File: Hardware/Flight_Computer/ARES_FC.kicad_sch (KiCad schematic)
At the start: 46 parts, among them J1 SWD, J2 TYPE-C-31-M-12, J4 5V, J5 GND, U1 STM32F401CCU6, U2 AMS1117-3.3, U3 BMP280, U4 BNO055, U5 W25Q32JVSS, Y1 16MHz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

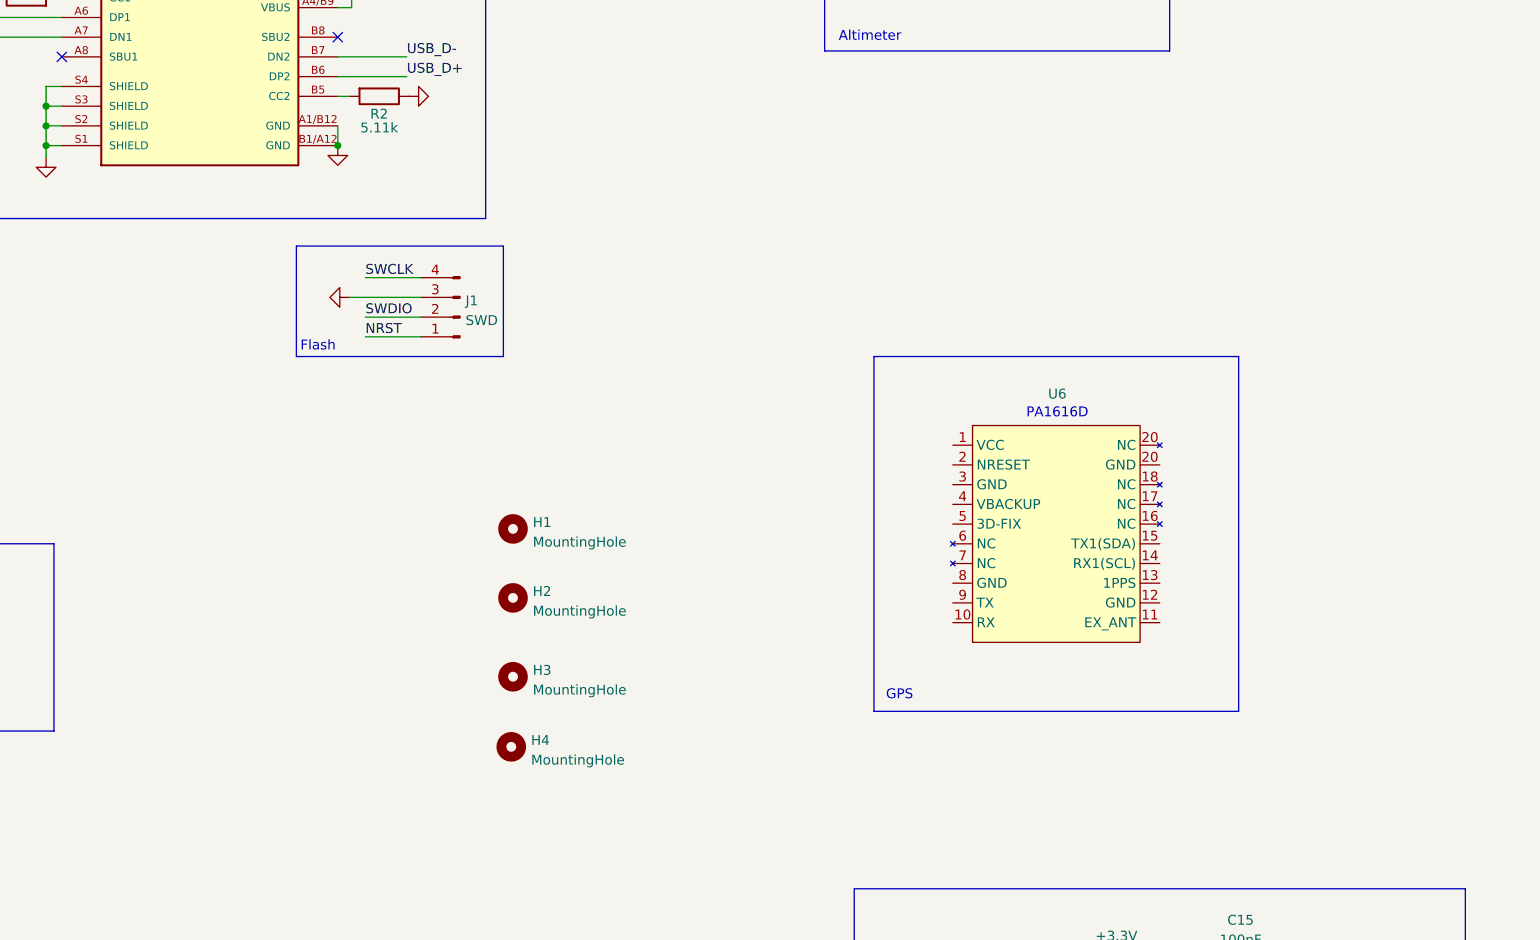
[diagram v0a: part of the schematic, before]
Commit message: started filling out GPS schematic
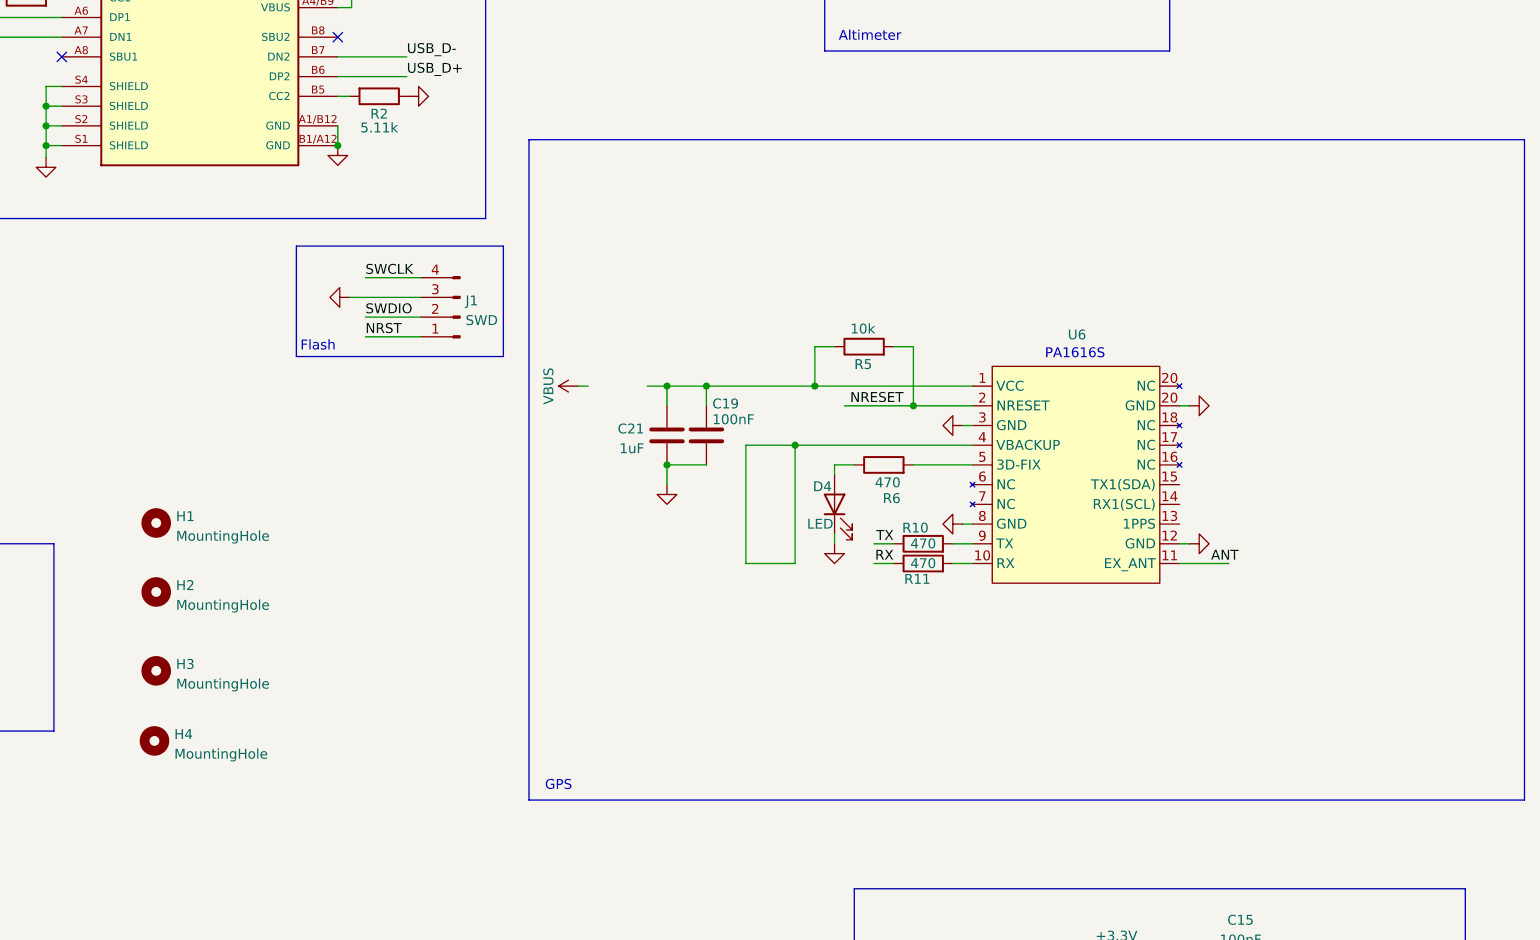
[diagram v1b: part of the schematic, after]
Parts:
- added C19: 100nF, Capacitor_SMD:C_0402_1005Metric, symbol Device:C
- added C21: 1uF, Capacitor_SMD:C_0402_1005Metric, symbol Device:C
- added D4: LED, LED_SMD:LED_0603_1608Metric, symbol Device:LED
- added R10, R11, R6: 470, Resistor_SMD:R_0402_1005Metric, symbol Device:R
- added R5: 10k, Resistor_SMD:R_0402_1005Metric, symbol Device:R
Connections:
- net GND: now also U6.12 (GND), U6.20 (NC), U6.3 (GND), U6.8 (GND), C19.2, C21.2, D4.1 (K)
- net at U6.1 (VCC): now also C19.1, C21.1, R5.1
- net at U6.10 (RX): now also R11.2
- net NRESET: now reaches U6.2 (NRESET)
- net NRESET: now also R5.2
- net at U6.5 (3D-FIX): now also R6.2
- net at U6.9 (TX): now also R10.2
- new net: D4.2 (A), R6.1
- new net RX: R11.1
- new net TX: R10.1
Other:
- note added: "PA1616S"
- note removed: "PA1616D"
- moved on the sheet: H1, H2, H3, H4, U6

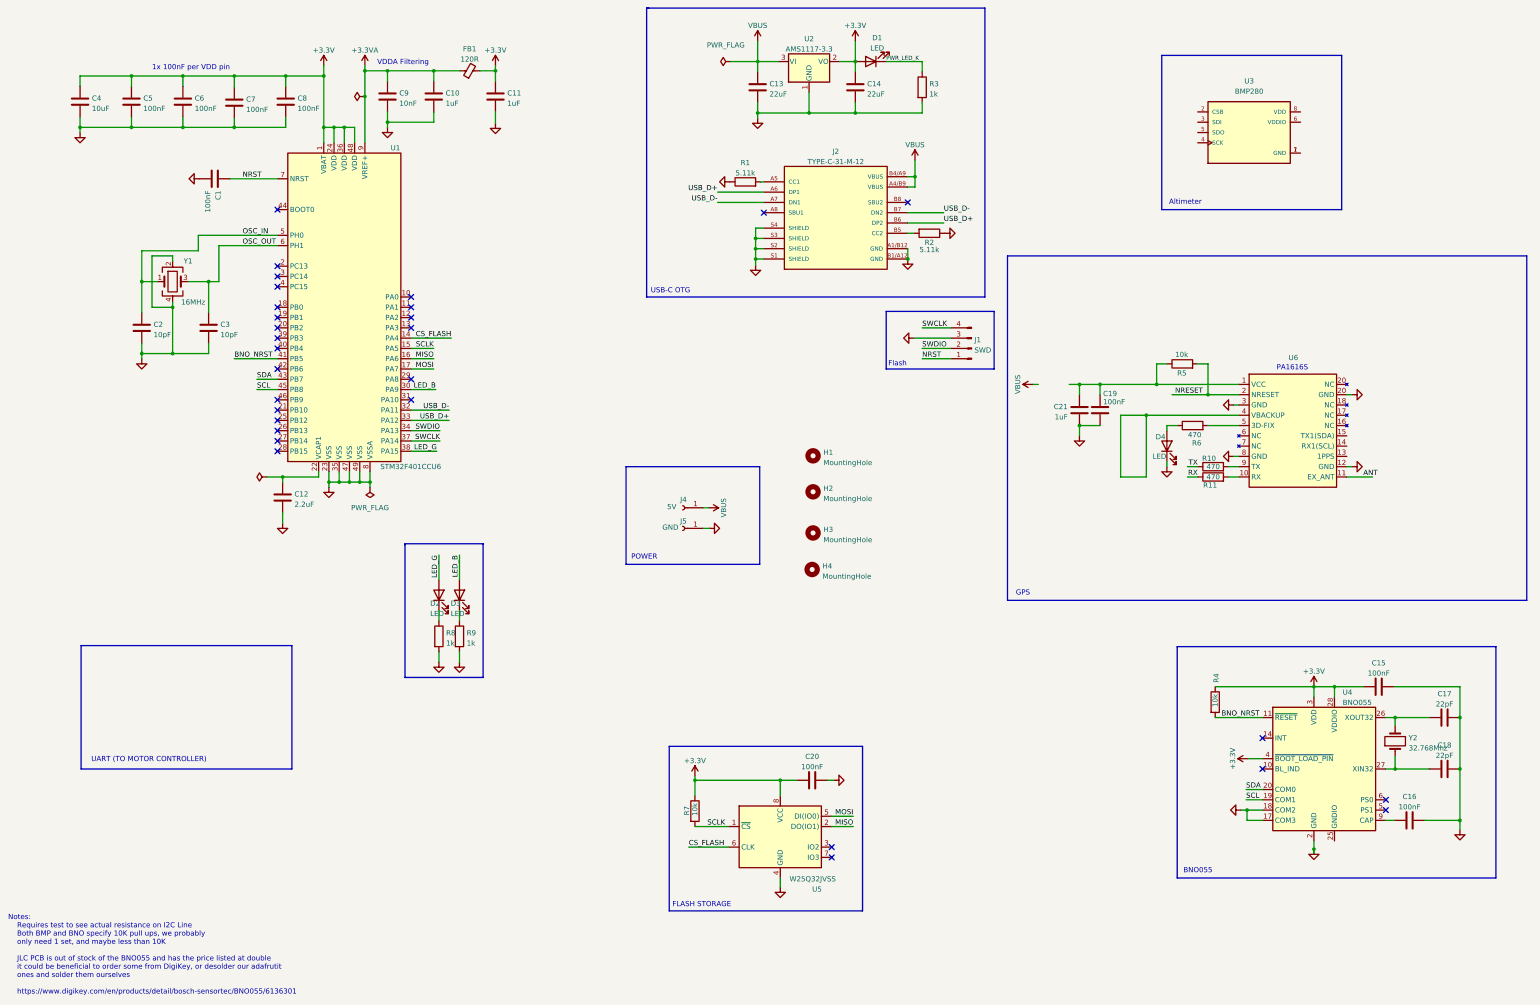
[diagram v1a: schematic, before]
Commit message: finished GPS schematic
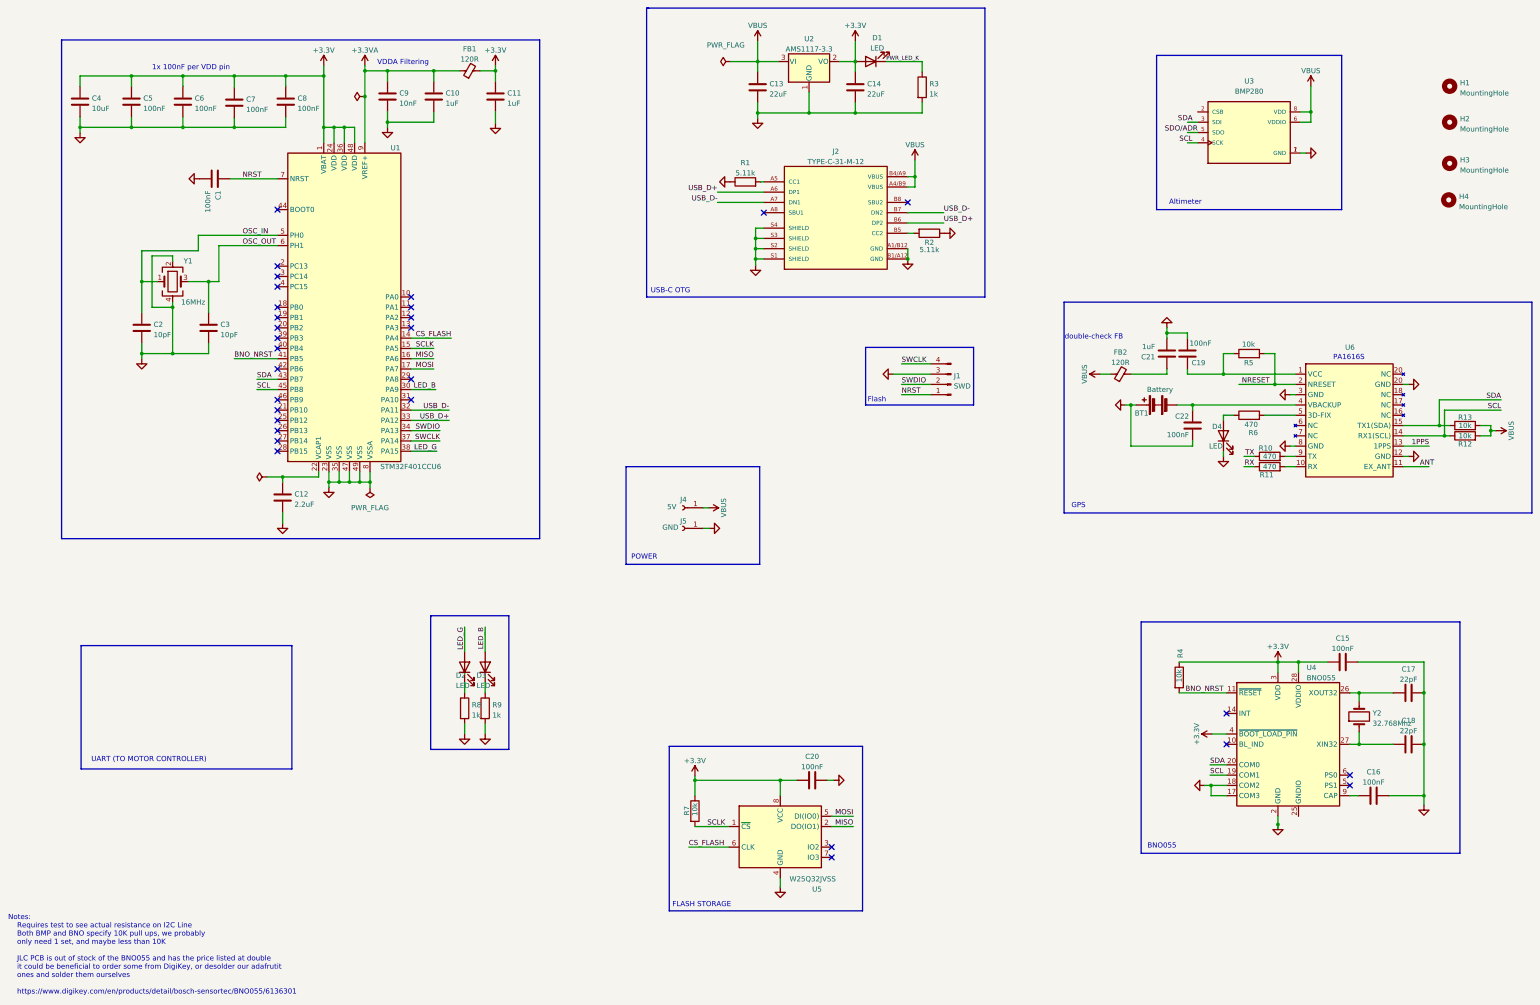
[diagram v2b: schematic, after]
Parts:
- added BT1: Battery, symbol Device:Battery
- added C22: 100nF, Capacitor_SMD:C_0402_1005Metric, symbol Device:C
- added FB2: 120R, Inductor_SMD:L_0603_1608Metric, symbol Device:FerriteBead_Small
- added R12, R13: 10k, symbol Device:R
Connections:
- net GND: now also U3.1 (GND), U3.7 (GND), BT1.1 (+), C22.2
- net SCL: now also U3.4 (SCK), U6.14 (RX1(SCL)), R12.1
- net SDA: now also U3.3 (SDI), U6.15 (TX1(SDA)), R13.1
- net VBUS: now also U3.6 (VDDIO), U3.8 (VDD), FB2.1, R12.2, R13.2
- net at C19.1, R5.1, U6.1 (VCC): no longer C21.1
- net 1PPS: now reaches U6.13 (1PPS)
- net at U6.4 (VBACKUP): now also BT1.2 (-), C22.1
- net SDO/ADR: now reaches U3.5 (SDO)
- new net: C21.1, FB2.2
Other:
- note added: "double-check FB"
- moved on the sheet: C15, C16, C17, C18, C19, C21, D2, D3, D4, H1, H2, H3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

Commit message: finished schematic for MBP280, GPS and UARTs
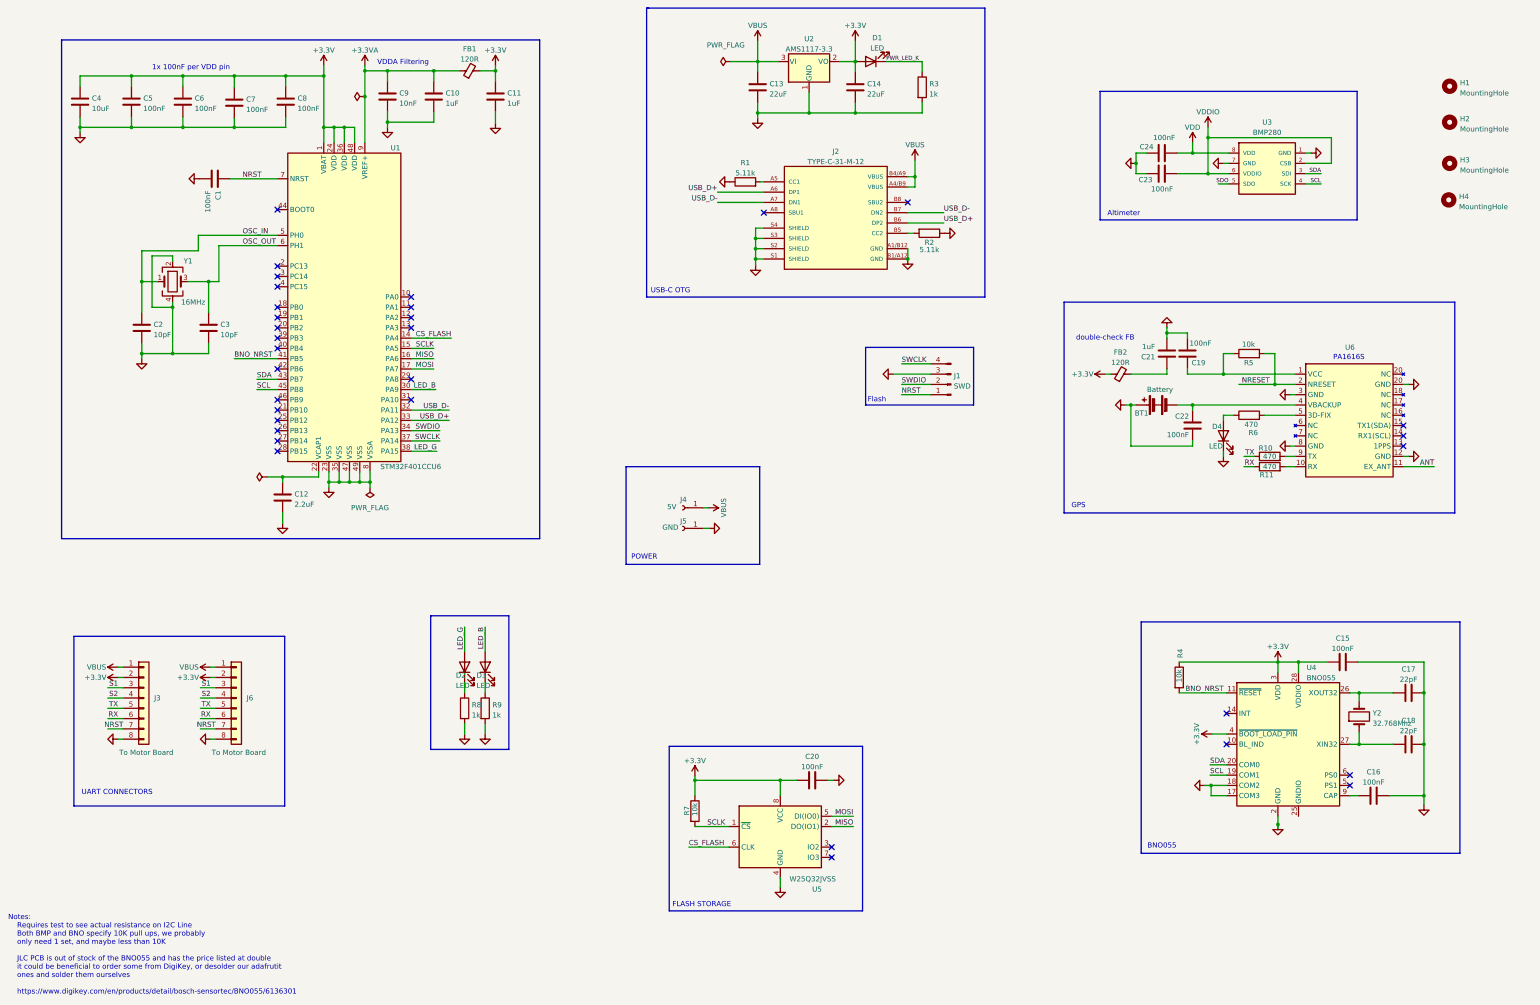
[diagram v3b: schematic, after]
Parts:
- removed R12, R13: 10k, symbol Device:R
- added C23, C24: 100nF, Capacitor_SMD:C_0402_1005Metric, symbol Device:C
- added J3, J6: To Motor Board, symbol Connector_Generic:Conn_01x08
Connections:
- net +3.3V: now also FB2.1, J3.2 (Pin_2), J6.2 (Pin_2)
- net ANT: now also U6.11 (EX_ANT)
- net GND: now also C23.1, C24.1, J3.8 (Pin_8), J6.8 (Pin_8)
- net NRST: now also J3.7 (Pin_7), J6.7 (Pin_7)
- net RX: now also J3.6 (Pin_6), J6.6 (Pin_6)
- net SCL: no longer U6.14 (RX1(SCL))
- net SDA: no longer U6.15 (TX1(SDA))
- net TX: now also J3.5 (Pin_5), J6.5 (Pin_5)
- net VBUS: now also J3.1 (Pin_1), J6.1 (Pin_1); no longer FB2.1, U3.6 (VDDIO), U3.8 (VDD)
- net VDDIO: now reaches U3.2 (CSB)
- net VDDIO: now also U3.6 (VDDIO), C23.2
- net 1PPS: no longer names the net of U6.13 (1PPS)
- net SDO/ADR renamed SDO
- new net S1: J3.3 (Pin_3), J6.3 (Pin_3)
- new net S2: J3.4 (Pin_4), J6.4 (Pin_4)
- new net VDD: C24.2, U3.8 (VDD)
- no-connect marks 30 -> 33
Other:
- note added: "UART CONNECTORS"
- note removed: "UART (TO MOTOR CONTROLLER)"

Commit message: Fixed "RCS Board Problems"
in RCS Board Problems Discord Thread.
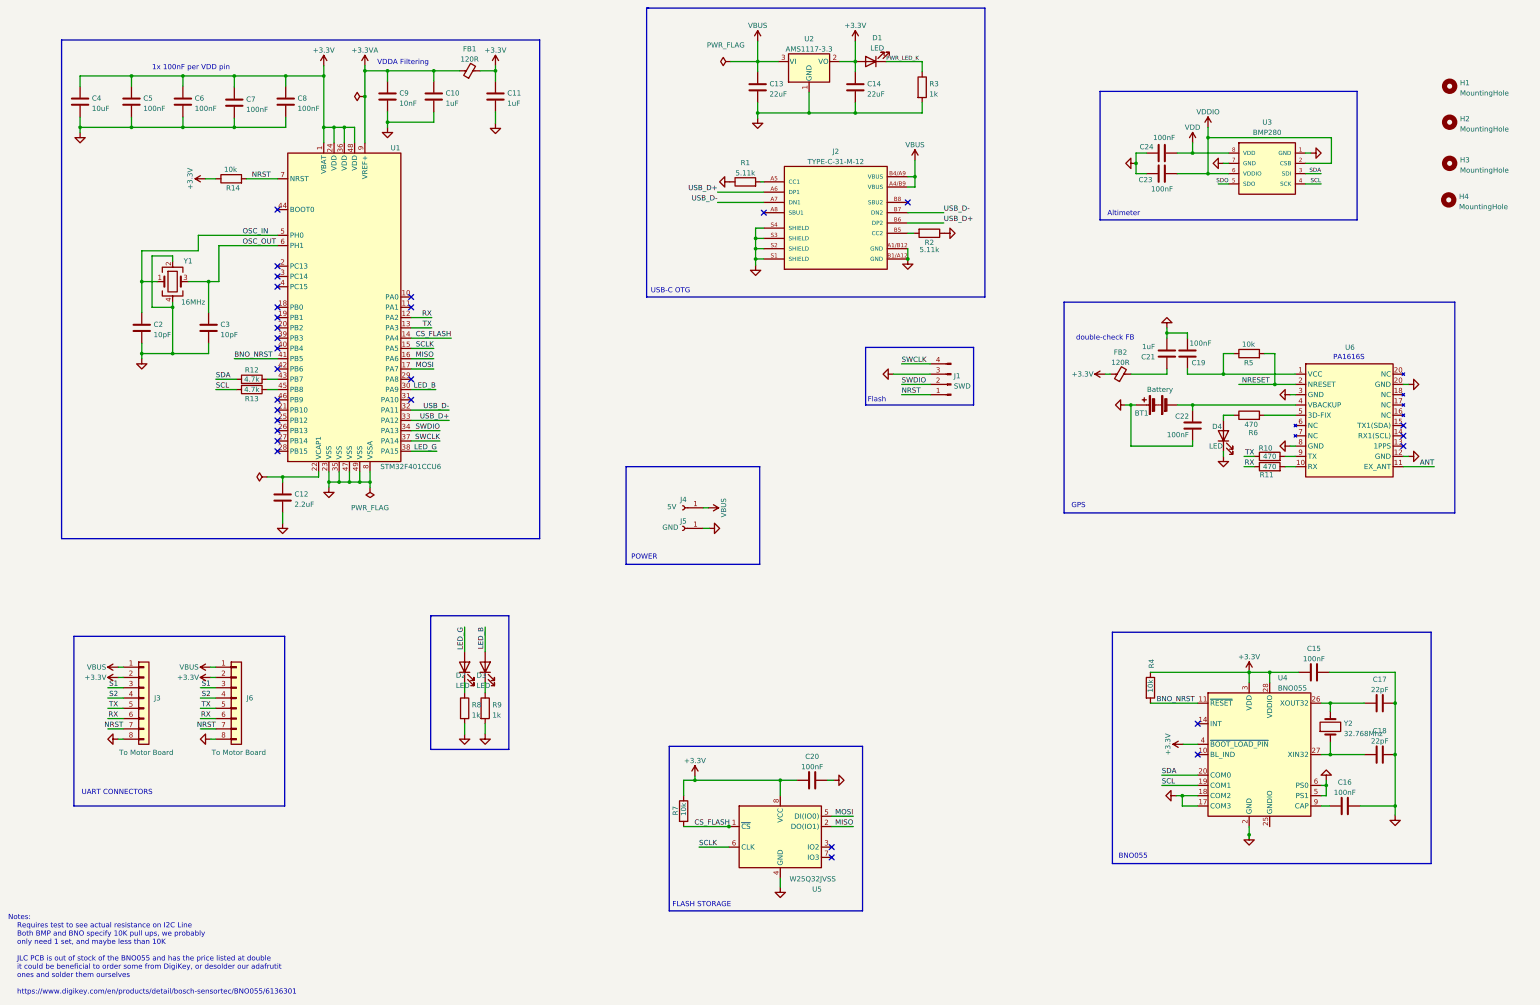
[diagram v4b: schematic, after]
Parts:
- removed C1: 100nF, Capacitor_SMD:C_0402_1005Metric, symbol Device:C
- added R12, R13: 4.7k, Resistor_SMD:R_0402_1005Metric, symbol Device:R
- added R14: 10k, Resistor_SMD:R_0402_1005Metric, symbol Device:R
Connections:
- net +3.3V: now also R14.1
- net CS_FLASH: now also R7.2, U5.1 (~{CS}); no longer U5.6 (CLK)
- net GND: now also U4.5 (PS1), U4.6 (PS0)
- net NRST: now also R14.2
- net RX: now also U1.12 (PA2)
- net SCL: now also R13.2; no longer U1.45 (PB8)
- net SCLK: now also U5.6 (CLK); no longer R7.2, U5.1 (~{CS})
- net SDA: now also R12.2; no longer U1.43 (PB7)
- net TX: now also U1.13 (PA3)
- new net: R13.1, U1.45 (PB8)
- new net: R12.1, U1.43 (PB7)
- no-connect marks 33 -> 29
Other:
- moved on the sheet: C15, C16, C17, C18, R4, R7, U4, Y2
